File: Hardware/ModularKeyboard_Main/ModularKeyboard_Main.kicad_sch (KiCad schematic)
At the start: 50 parts, among them J1 Conn_01x03, J2 Conn_01x03, J3 SM04B-SRSS-TB(LF)(SN), SW0 SW_SPST, SW1 SW_SPST, SW10 SW_SPST, SW11 SW_SPST, SW12 SW_SPST, SW13 SW_SPST, SW14 SW_SPST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

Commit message: Completed most wiring
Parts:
- added H1, H2, H3, H4: MountingHole, MountingHole:MountingHole_2.2mm_M2, symbol Mechanical:MountingHole
- added J3, J4: Conn_01x03, CUSTOM:PG-3P-2.5, symbol Connector_Generic:Conn_01x03
- added J6: SM04B-SRSS-TB(LF)(SN), SM04B-SRSS-TB_LF__SN:JST_SM04B-SRSS-TB(LF)(SN), symbol SM04B-SRSS-TB_LF__SN_:SM04B-SRSS-TB(LF)(SN)
- added OL1: OLED, kbd-master:OLED_v2, symbol kbd:OLED
- added R6, R7: DNP, Resistor_SMD:R_0402_1005Metric, symbol Device:R_Small
- renumbered J3 to J5
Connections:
- net MISO is gone; now on net CE: J2.2 (Pin_2)
- net MOSI is gone; now on net SPI1_MISO: J2.3 (Pin_3)
- net SCLK is gone; now on net SPI1_SCK: J1.1 (Pin_1)
- net ~{CE} is gone; now on net CE: U1.15 (~{CE}), U3.15 (~{CE})
- net ~{PL} is gone; now on net PL: U1.1 (~{PL}), U3.1 (~{PL})
- net ~{SS} is gone; now on net PL: J2.1 (Pin_1)
- net +3V3: now also J3.1 (Pin_1), J6.1, OL1.3 (VCC)
- net GND: now also J3.2 (Pin_2), J6.3, OL1.4 (GND), R6.1, R7.1
- net SPI1_MISO: now also J4.1 (Pin_1)
- net SPI1_SCK: now also J3.3 (Pin_3)
- net SPI2_MISO: now also U2.27 (PB14); no longer U2.37 (PA14)
- net SPI2_MOSI: now also U2.28 (PB15); no longer U2.38 (PA15)
- net SPI2_SCK: now also U2.26 (PB13); no longer U2.34 (PA13)
- net MCU_D-: now reaches R2.1, U2.32 (PA11)
- net MCU_D+: now reaches R3.1, U2.33 (PA12)
- net PL: now reaches U2.39 (PB3)
- net PL: now also J4.3 (Pin_3)
- net CE: now reaches U2.40 (PB4)
- net CE: now also J4.2 (Pin_2)
- net I2C1_SCL: now reaches U2.42 (PB6)
- net I2C1_SCL: now also OL1.2 (SCL)
- net I2C1_SDA: now reaches U2.43 (PB7)
- net I2C1_SDA: now also OL1.1 (SDA)
- net at J5.S1 (SHIELD), J5.S2 (SHIELD): now also R6.2
- new net: J6.S1 (SHIELD), J6.S2 (SHIELD), R7.2
- new net SWCLK: J6.4, U2.37 (PA14)
- new net SWDIO: J6.2, U2.34 (PA13)
- no-connect marks 39 -> 28
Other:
- note added: "Connectors"
- note added: "SWD"
- note added: "UNIFIED C3"
- note removed: "Daughterboard"
- note removed: "Pogo pins"
- moved on the sheet: J1, J2, J5, MH1, MH2, MH3, MH4

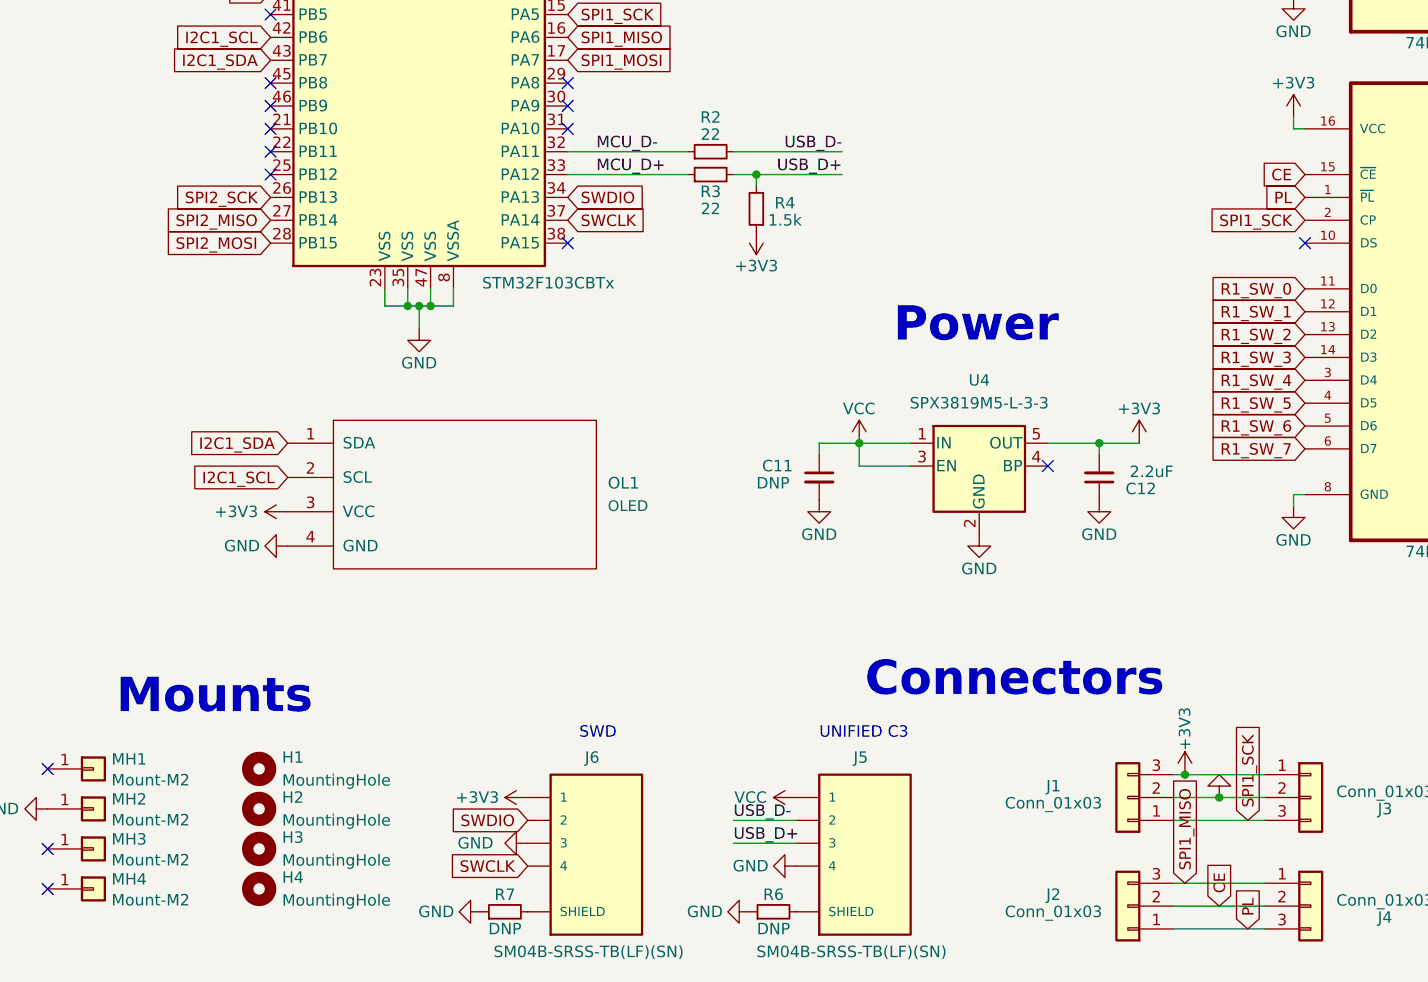
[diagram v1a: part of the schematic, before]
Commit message: Completed wiring v0.1 -- add bom
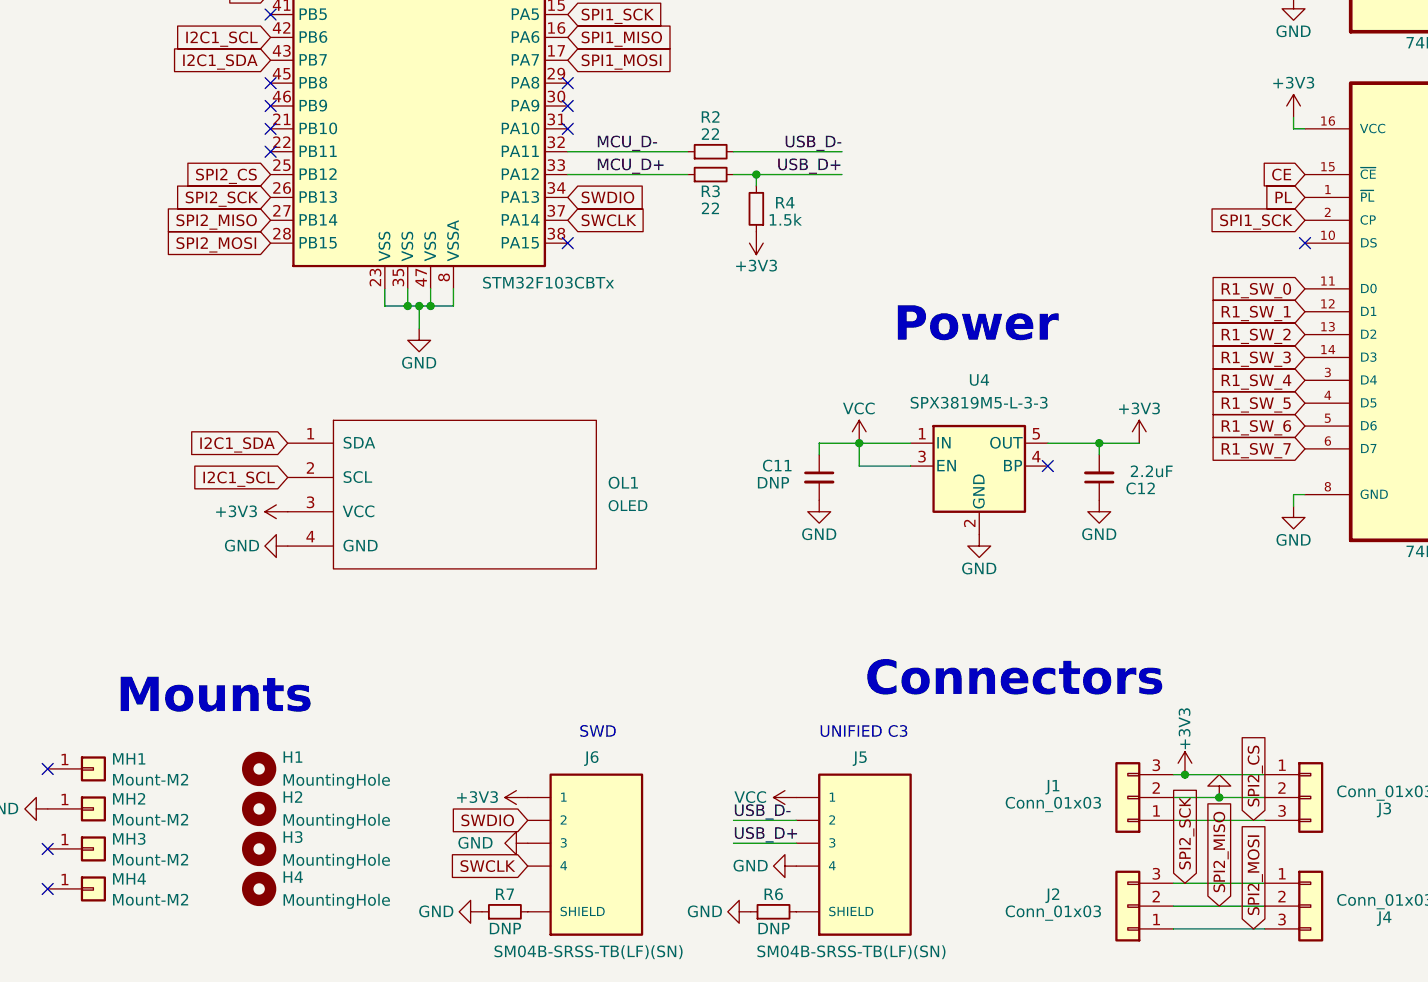
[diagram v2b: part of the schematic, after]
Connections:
- net CE: no longer J2.2 (Pin_2), J4.2 (Pin_2)
- net PL: no longer J2.1 (Pin_1), J4.3 (Pin_3)
- net SPI1_MISO: no longer J2.3 (Pin_3), J4.1 (Pin_1)
- net SPI1_SCK: no longer J1.1 (Pin_1), J3.3 (Pin_3)
- net SPI2_MISO: now also J2.2 (Pin_2), J4.2 (Pin_2)
- net SPI2_MOSI: now also J2.1 (Pin_1), J4.3 (Pin_3)
- net SPI2_SCK: now also J2.3 (Pin_3), J4.1 (Pin_1)
- net SPI2_CS: now reaches U2.25 (PB12)
- net SPI2_CS: now also J1.1 (Pin_1), J3.3 (Pin_3)
- no-connect marks 28 -> 27

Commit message: Completed v0.1
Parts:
- C11: value DNP -> 2.2uF
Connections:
- net SWCLK: now also J6.2; no longer J6.4
- net SWDIO: now also J6.4; no longer J6.2
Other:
- moved on the sheet: H1, H2, H3, H4, MH1, MH2, MH3, MH4
